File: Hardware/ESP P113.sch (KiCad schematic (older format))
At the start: 89 parts, among them J1 Gain_L_Ex, J2 Gain_R_Ex, J3 L_In, J4 R_In, J5 HPOut, J6 PE, J7 AC_L, J8 AC_N, J9 GND_Audio, K1 G6A-234P-ST15-US-DC24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

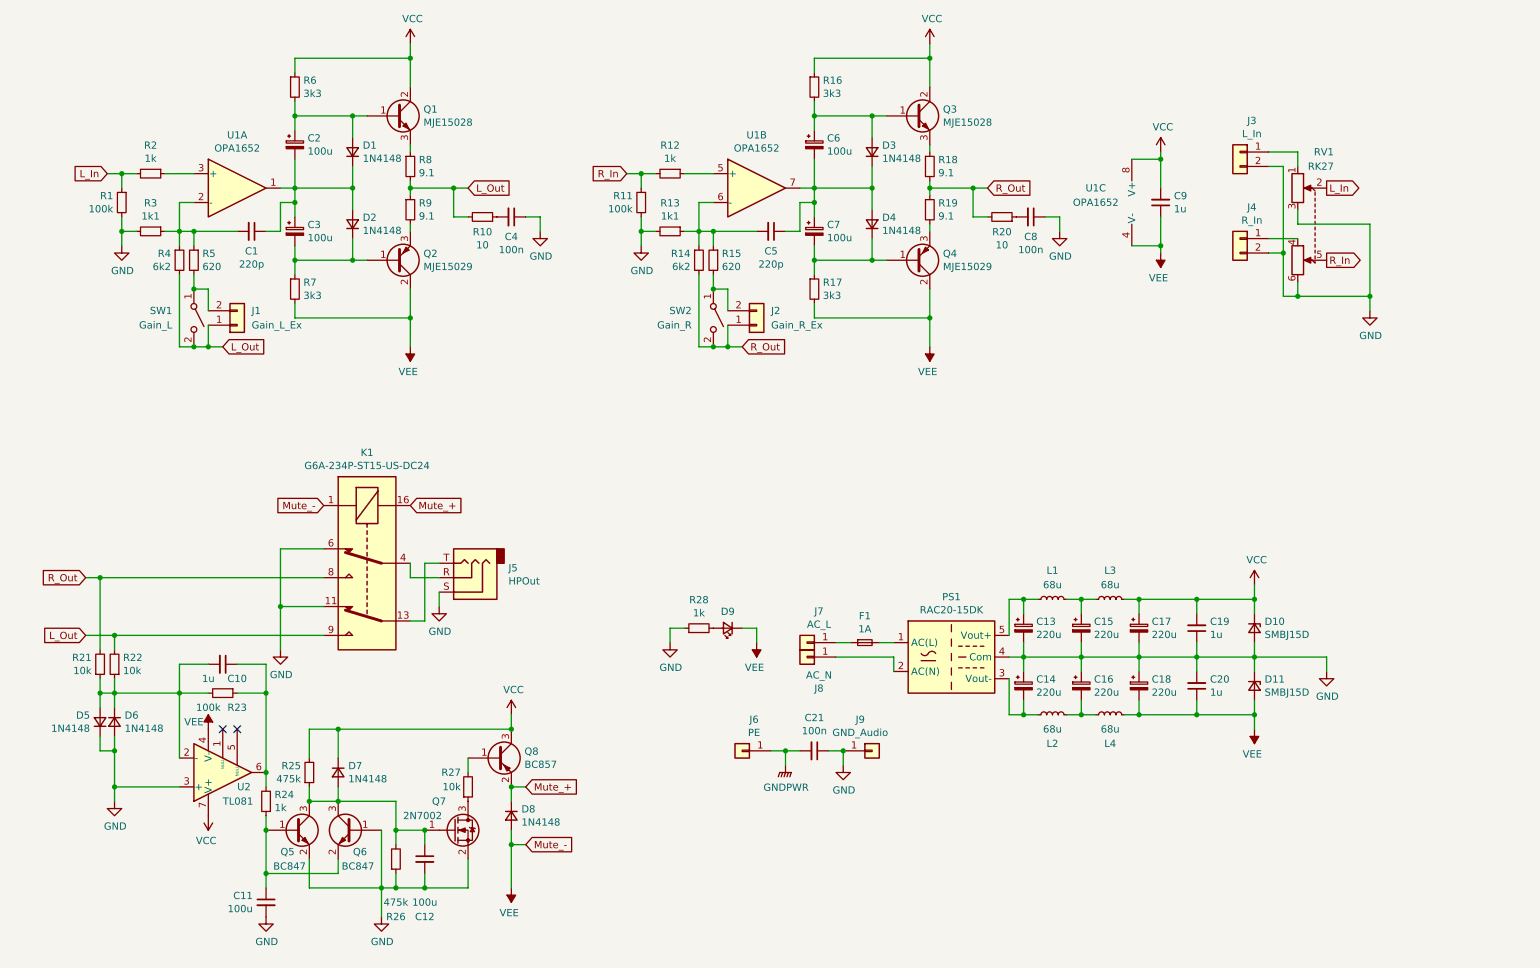
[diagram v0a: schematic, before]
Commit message: Updated layout, re-added BOM.
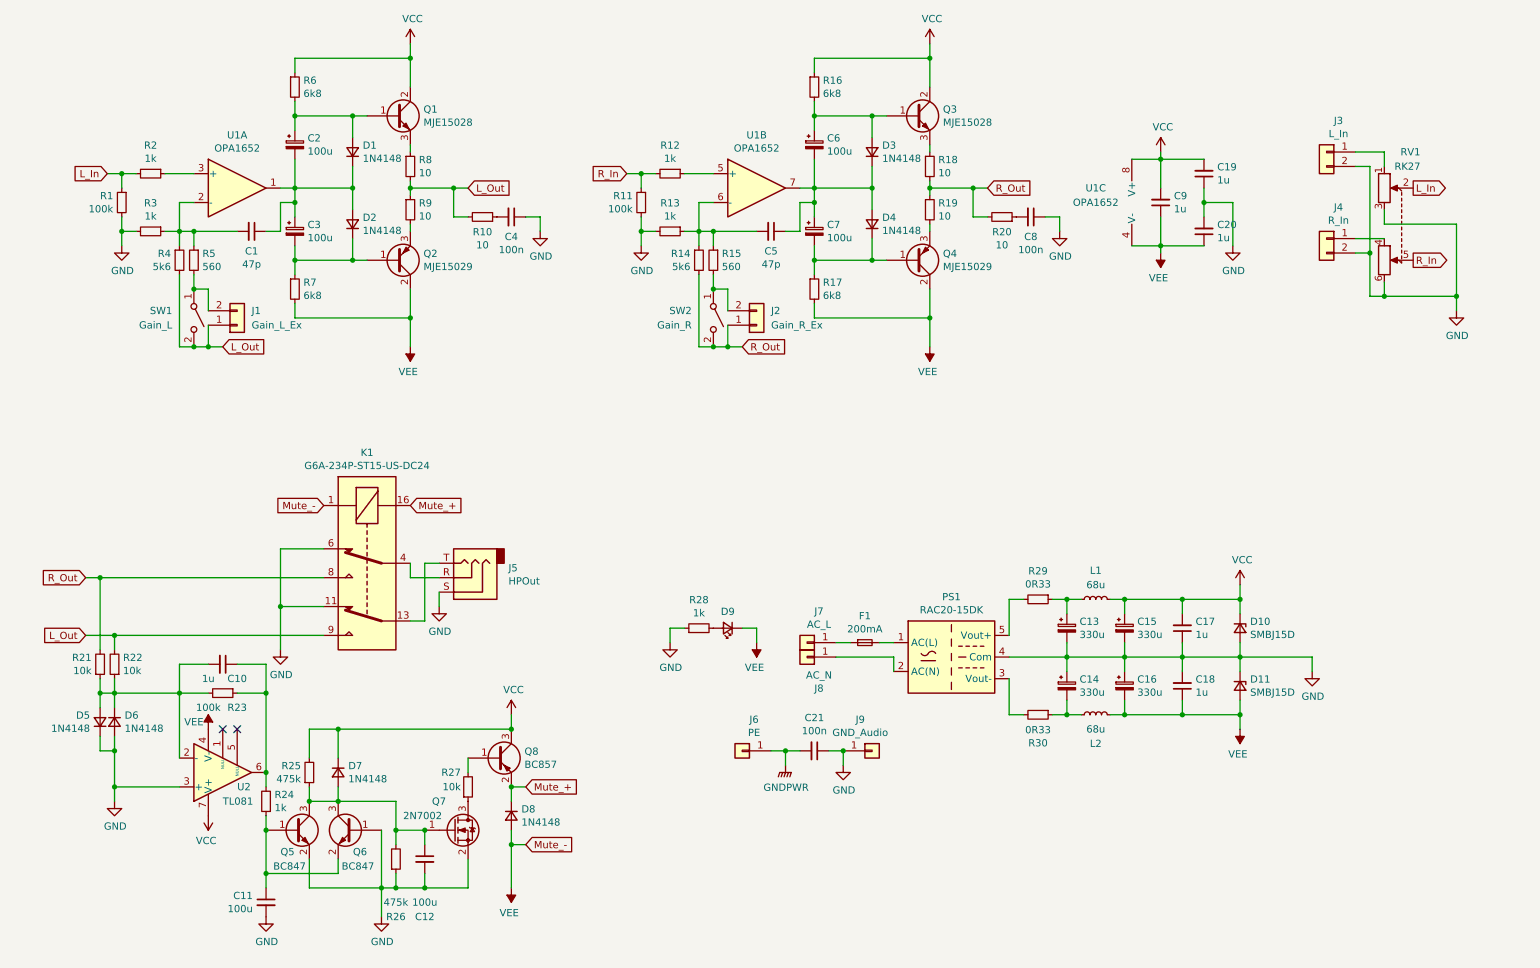
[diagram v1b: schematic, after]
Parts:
- removed C17, C18: 220u, Capacitor_THT:CP_Radial_D10.0mm_P5.00mm, symbol Device:CP_Small
- removed L3, L4: 68u, Inductor_THT:L_Radial_D8.7mm_P5.00mm_Fastron_07HCP, symbol Device:L_Small
- added C19, C20: 1u, Capacitor_SMD:C_1206_3216Metric_Pad1.33x1.80mm_HandSolder, symbol Device:C_Small
- added R29, R30: 0R33, Resistor_SMD:R_2512_6332Metric_Pad1.40x3.35mm_HandSolder, symbol Device:R_Small
- C1, C5: value 220p -> 47p
- C13, C14, C15, C16: value 220u -> 330u; footprint Capacitor_THT:CP_Radial_D10.0mm_P5.00mm -> Capacitor_THT:CP_Radial_D8.0mm_P3.50mm
- C21: footprint Capacitor_THT:C_Rect_L18.0mm_W6.0mm_P15.00mm_FKS3_FKP3 -> Capacitor_THT:C_Rect_L26.5mm_W8.5mm_P22.50mm_MKS4
- C4, C8: footprint Capacitor_SMD:C_1206_3216Metric_Pad1.33x1.80mm_HandSolder -> Capacitor_SMD:C_1210_3225Metric_Pad1.33x2.70mm_HandSolder
- F1: value 1A -> 200mA
- R13, R3: value 1k1 -> 1k
- R14, R4: value 6k2 -> 5k6
- R15, R5: value 620 -> 560
- R16, R17, R6, R7: value 3k3 -> 6k8
- R18, R19, R8, R9: value 9.1 -> 10
- renumbered C19 to C17, C20 to C18
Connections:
- net GND: now also C19.1, C20.2
- net VCC: now also C15.1, L1.2, C19.2
- net VEE: now also C16.2, L2.2, C20.1
- net at C13.1, L1.1: now also R29.1; no longer PS1.5 (Vout+)
- net at C14.2, L2.1: now also R30.1; no longer PS1.3 (Vout-)
- new net: PS1.3 (Vout-), R30.2
- new net: PS1.5 (Vout+), R29.2
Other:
- moved on the sheet: C13, C14, C15, C16, C17, C18, D10, D11, J3, J4, L1, L2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

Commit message: Added RFI filter.
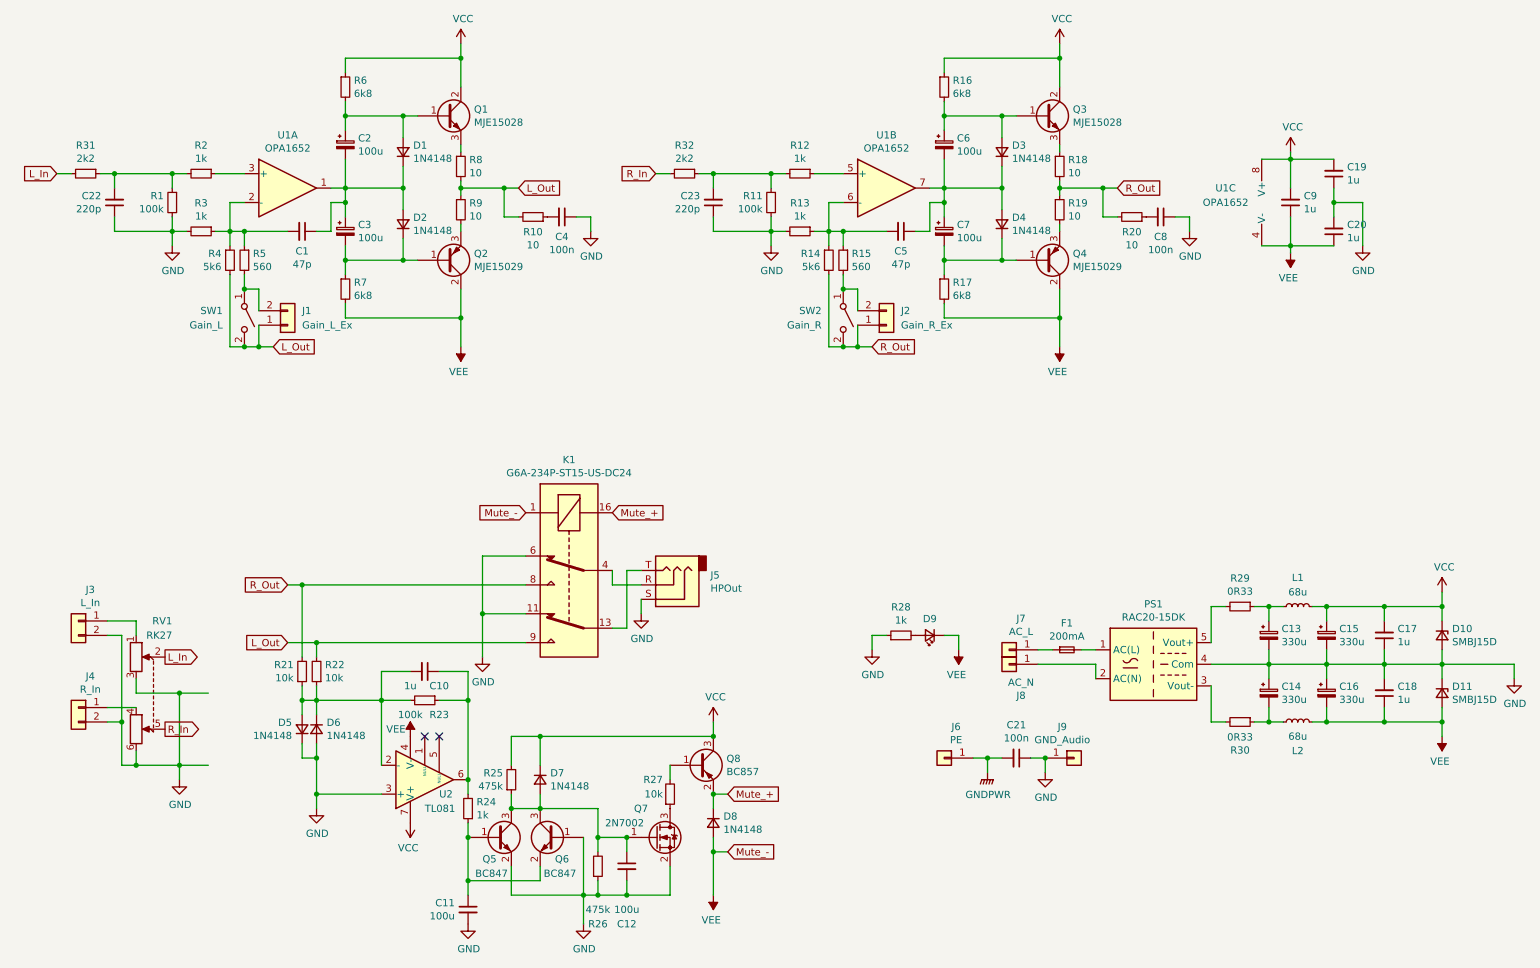
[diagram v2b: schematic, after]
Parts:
- added C22, C23: 220p, Capacitor_SMD:C_1206_3216Metric_Pad1.33x1.80mm_HandSolder, symbol Device:C_Small
- added R31, R32: 2k2, Resistor_SMD:R_1206_3216Metric_Pad1.30x1.75mm_HandSolder, symbol Device:R_Small
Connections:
- net GND: now also C22.1, C23.1
- net L_In: now also R31.2; no longer R1.1, R2.2
- net R_In: now also R32.2; no longer R11.1, R12.2
- new net: C22.2, R1.1, R2.2, R31.1
- new net: C23.2, R11.1, R12.2, R32.1
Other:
- moved on the sheet: C1, C10, C11, C12, C13, C14, C15, C16, C17, C18, C19, C2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
